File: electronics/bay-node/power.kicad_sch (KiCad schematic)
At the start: 23 parts, among them J1 24V IN, J2 24V OUT, Q1 SUD50P06-15, U1 LMR51635YDDCR, U2 AMS1117-3.3

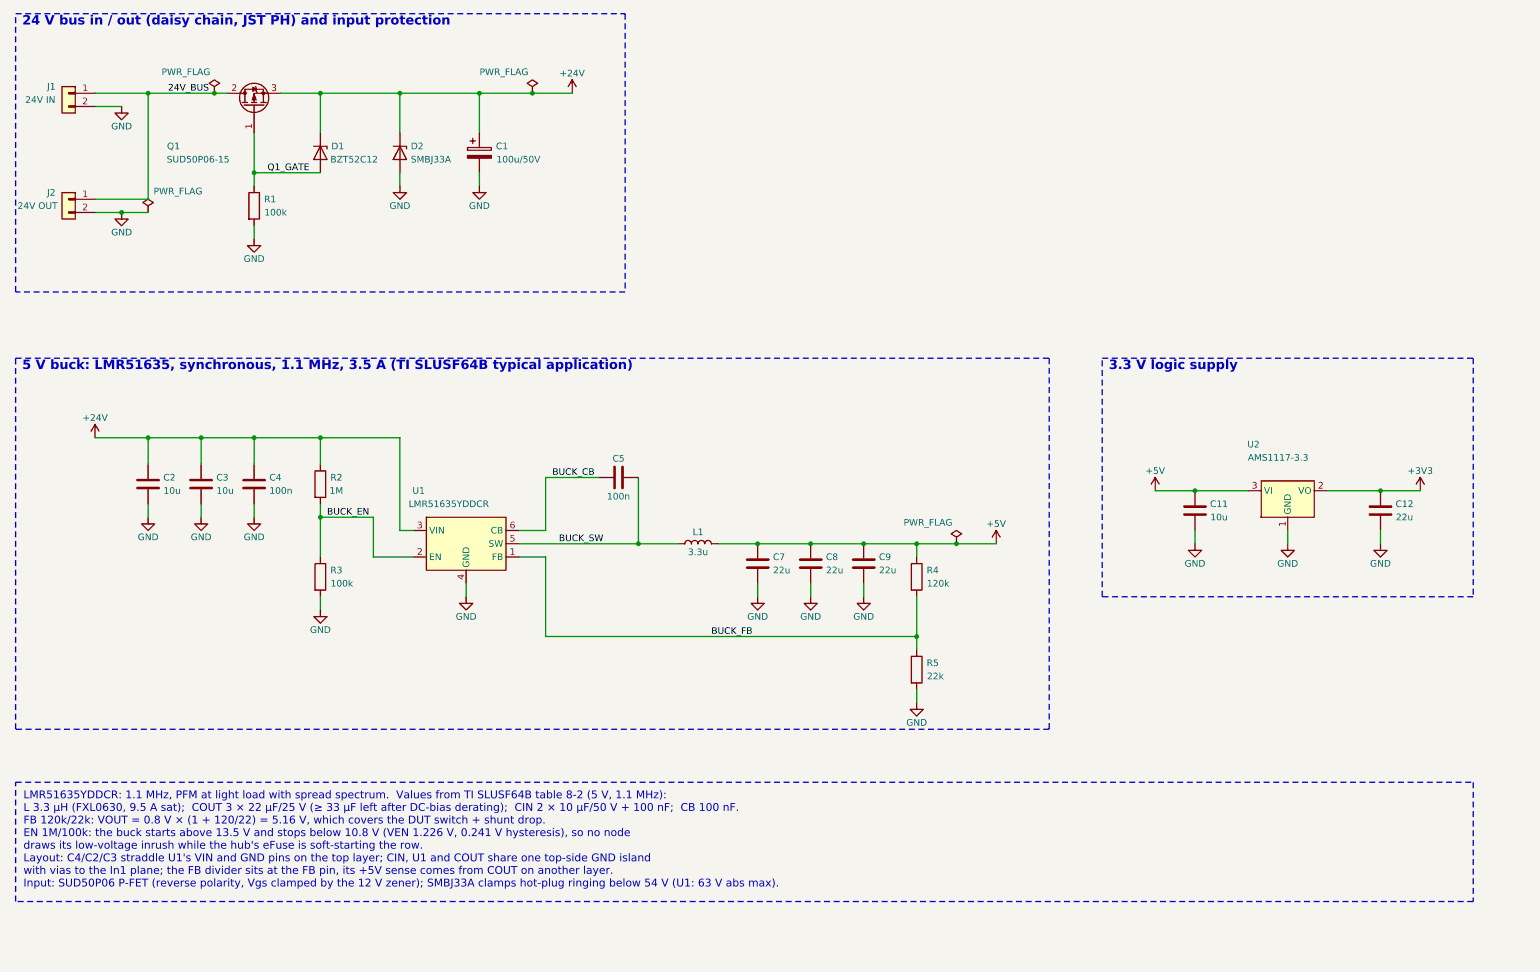
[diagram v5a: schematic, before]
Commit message: Bay node v0.5: 6-pin row cable with CAN and POS
The row cable becomes the docs/can.md contract: J1 (ROW IN, left) and J2 (ROW OUT,
right) are 6-pin JST PH S6B-PH-SM4-TB, +24 V, GND, CAN_H, CAN_L, GND, POS, with
pin 1 to the rear on the left edge and to the front on the right edge.

- Rack bus sheet: TCAN1044AV (VCC 5 V, VIO 3.3 V, STB low) right on the pair,
  which runs straight J1 -> J2 with no termination (stubs 1.8 / 2.3 mm),
  PESD2CAN on the tap; POS in through 10k + BAT54S + 100k pull-down, POS out
  through 10k + BAT54S.  TWAI on IO18/IO17, POS on IO16 (in) and IO35 (out).
- The input stage also takes a 20 / 28 V USB-C PD supply (notes on the Power
  sheet and in docs/electronics.md).
- Re-placed for In2 power only and autorouted: ERC 0, DRC 0, unconnected 0,
  parity 0 (kicad-cli and Konnect); no track on In1 or In2.
- JLC_CPL_FIX gains the rack bus parts, fitted on the EasyEDA footprints:
  S6B 180 deg, TCAN1044AV 270 deg, PESD2CAN and BAT54S 180 deg (they also apply
  to the power hub's row connectors, transceiver and clamps).
- Firmware: hwtr,rack-bus binding, TWAI pinctrl and node in the bay_node
  devicetree, check_pinmap and the README table; DevKitC moves POS_OUT to IO21,
  StampS3 disables the bus.  bay_node, DevKitC and StampS3 builds pass.
- Mechanics: the cable windows in the tray walls and the ladders widen to
  17 mm for the PHR-6 plug.  The viewer and the notice draw a 6-wire jumper.
- BOM: 6-pin jumpers; JLC_SINCE_QUOTE adds rev 0.5's parts and three extended
  part types to the node's quoted order (indicative, re-quote).

Regenerated: KiCad project, fab outputs, renders, schematic PDF, viewer GLB,
tray and ladder STLs, parts.glb, rack.json, bom/*.

Co-Authored-By: Claude Opus 5.5 <noreply@anthropic.com>
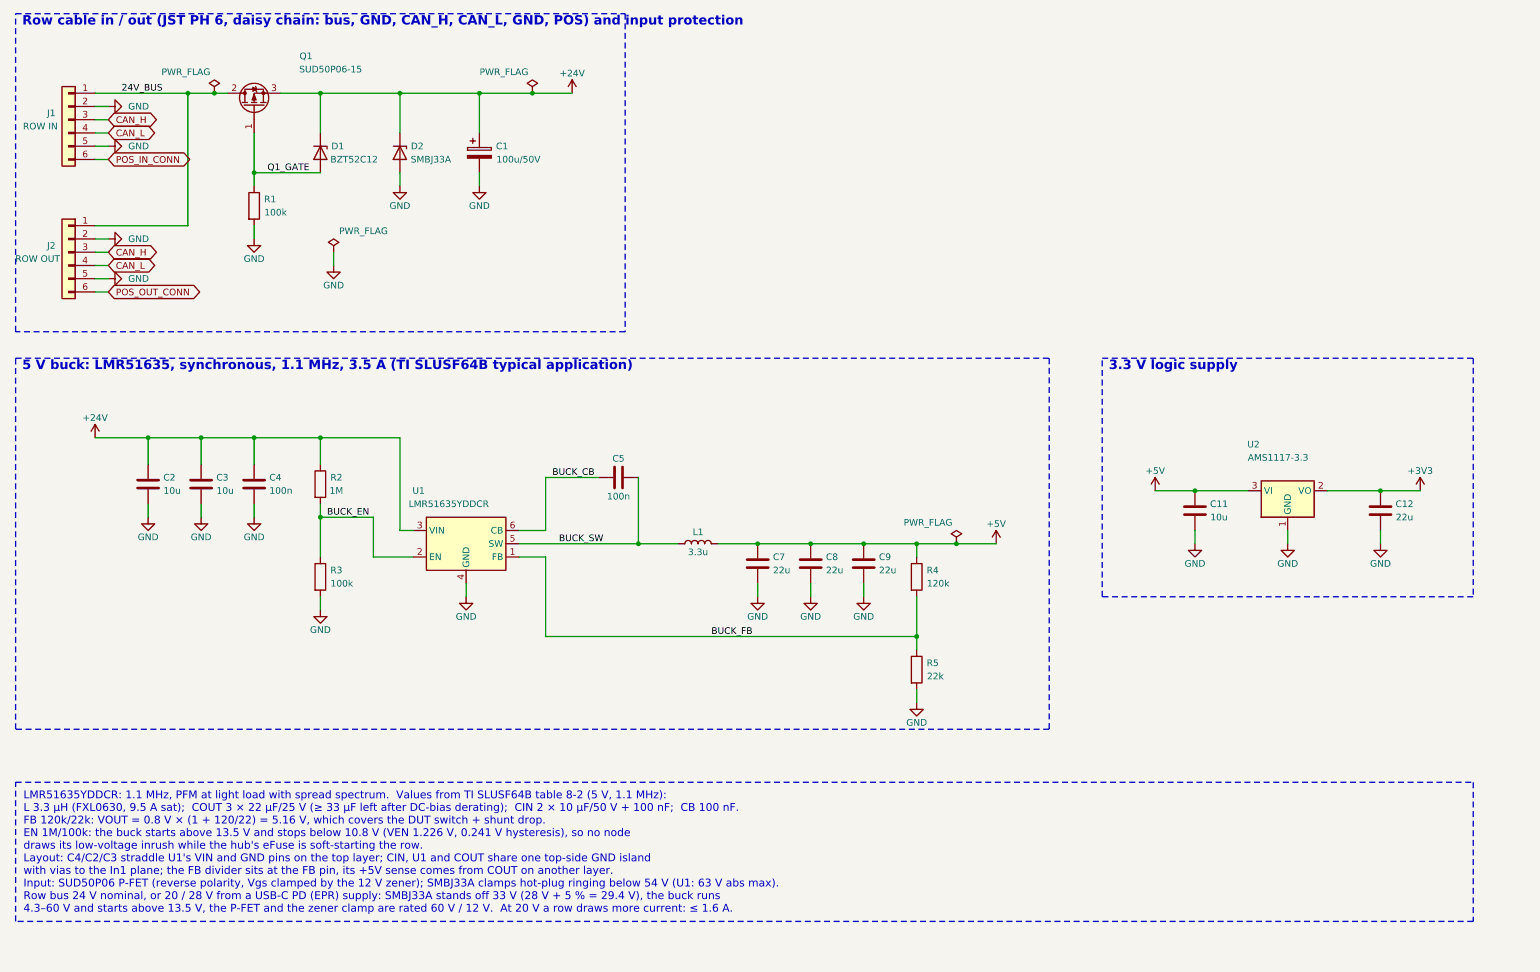
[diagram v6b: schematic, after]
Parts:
- J1: value 24V IN -> ROW IN; footprint Connector_JST:JST_PH_S2B-PH-SM4-TB_1x02-1MP_P2.00mm_Horizontal -> Connector_JST:JST_PH_S6B-PH-SM4-TB_1x06-1MP_P2.00mm_Horizontal; symbol Connector_Generic:Conn_01x02 -> Connector_Generic:Conn_01x06; LCSC C295747 -> C265405; MPN S2B-PH-SM4-TB(LF)(SN) -> S6B-PH-SM4-TB(LF)(SN)
- J2: value 24V OUT -> ROW OUT; footprint Connector_JST:JST_PH_S2B-PH-SM4-TB_1x02-1MP_P2.00mm_Horizontal -> Connector_JST:JST_PH_S6B-PH-SM4-TB_1x06-1MP_P2.00mm_Horizontal; symbol Connector_Generic:Conn_01x02 -> Connector_Generic:Conn_01x06; LCSC C295747 -> C265405; MPN S2B-PH-SM4-TB(LF)(SN) -> S6B-PH-SM4-TB(LF)(SN)
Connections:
- net GND: now also J1.5 (Pin_5), J2.5 (Pin_5)
- new net CAN_H: J1.3 (Pin_3), J2.3 (Pin_3)
- new net CAN_L: J1.4 (Pin_4), J2.4 (Pin_4)
- new net POS_IN_CONN: J1.6 (Pin_6)
- new net POS_OUT_CONN: J2.6 (Pin_6)
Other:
- note added: "Row cable in / out (JST PH 6, daisy chain: bus, GND, CAN_H, CAN_L, GND, POS) and input protection"
- note removed: "24 V bus in / out (daisy chain, JST PH) and input protection"

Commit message: Bay node v0.5: VRACK, GCT USB-C, VBUS caps on the ESD parts
Follows the power box's switch to USB-C PD (docs/can.md on the power-box branch):

- Pin 1 of the row cable is VRACK (20 V, or 28 V EPR): the net 24V_BUS becomes
  VRACK and +24V (after the P-FET) becomes VIN, in the schematic, the zones and
  the netclass patterns.  The input stage already takes 20-28 V.
- J3/J4 become the GCT USB4105-GF-A-120 (catalog usbc5a, LCSC C5184243), the
  part the user approved for the hub.  KiCad 10 ships its 3D model.  The pads
  sit 0.365 mm closer to the footprint origin than the HRO's, so the hand-drawn
  USB High-Speed tracks move with them (both lines of each pair alike, so the
  matching holds).  A board rule allows the footprint's own 0.19 mm between its
  GND pads and its pegs, the same rule the hub uses.
- Konnect's open point from v0.4: C25 and C26 (100 nF) on U4's and U8's VBUS.
- JLC_CPL_FIX: C5184243 at 0 deg, -1.30 mm y (EasyEDA fit, residual 0).
- JLC_SINCE_QUOTE: +$2.38 of parts per board ($38.10 for the 16 quoted).

ERC 0, DRC 0, unconnected 0, parity 0; Konnect's design review shows only the
known per-sheet false positives.  CAN stubs to U11: 2.2 / 7.9 mm.

Co-Authored-By: Claude Opus 5.5 <noreply@anthropic.com>
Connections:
- net +24V renamed VIN
- net 24V_BUS renamed VRACK
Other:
- title: Bay node — 24 V input, 5 V buck, 3.3 V LDO -> Bay node — VRACK input (20–28 V), 5 V buck, 3.3 V LDO
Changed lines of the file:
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@@
 	(paper "A3")
 	(title_block
-		(title "Bay node — 24 V input, 5 V buck, 3.3 V LDO")
+		(title "Bay node — VRACK input (20–28 V), 5 V buck, 3.3 V LDO")
 		(rev "0.5")
 		(company "hw-testing-rack")
@@
 		)
 	)
-	(symbol
-		(lib_id "power:+24V")
-		(at 121.92 30.48 0)
-		(unit 1)
-		(exclude_from_sim no)
-		(in_bom yes)
-		(on_board yes)
-		(dnp no)
+	(label "VIN"
+		(at 121.92 30.48 90)
 		(fields_autoplaced yes)
-		(property "Reference" "#PWR02021"
-			(at 121.92 30.48 0)
-			(effects
-				(font
-					(size 1.27 1.27)
-				)
-				(hide yes)
-			)
-		)
-		(property "Value" "+24V"
-			(at 121.92 26.67 0)
-			(effects
-				(font
-					(size 1.27 1.27)
-				)
-			)
-		)
-		(property "Footprint" ""
-			(at 121.92 30.48 0)
-			(effects
-				(font
-					(size 1.27 1.27)
-				)
-				(hide yes)
-			)
-		)
-		(property "Datasheet" ""
-			(at 121.92 30.48 0)
-			(effects
-				(font
-					(size 1.27 1.27)
-				)
-				(hide yes)
-			)
-		)
-		(property "Description" ""
-			(at 121.92 30.48 0)
-			(effects
-				(font
-					(size 1.27 1.27)
-				)
-				(hide yes)
-			)
-		)
-		(pin "1"
-		)
-		(instances
-			(project "bay-node"
-				(path "/76847c0c-2f76-566c-8109-428b2bf58b3f/6bdbf57d-f796-52cd-9884-75545352918b"
-					(reference "#PWR02021")
-					(unit 1)
-				)
+		(effects
+			(font
+				(size 1.27 1.27)
 			)
+			(justify left bottom)
 		)
 	)
-	(symbol
-		(lib_id "power:+24V")
-		(at 30.48 96.52 0)
-		(unit 1)
-		(exclude_from_sim no)
-		(in_bom yes)
-		(on_board yes)
-		(dnp no)
+	(label "VIN"
+		(at 30.48 96.52 90)
 		(fields_autoplaced yes)
-		(property "Reference" "#PWR02022"
-			(at 30.48 96.52 0)
-			(effects
-				(font
-					(size 1.27 1.27)
-				)
-				(hide yes)
-			)
-		)
-		(property "Value" "+24V"
-			(at 30.48 92.71 0)
-			(effects
-				(font
-					(size 1.27 1.27)
-				)
-			)
-		)
-		(property "Footprint" ""
-			(at 30.48 96.52 0)
-			(effects
-				(font
-					(size 1.27 1.27)
-				)
-				(hide yes)
-			)
-		)
-		(property "Datasheet" ""
-			(at 30.48 96.52 0)
-			(effects
-				(font
-					(size 1.27 1.27)
-				)
-				(hide yes)
-			)
-		)
-		(property "Description" ""
-			(at 30.48 96.52 0)
-			(effects
-				(font
-					(size 1.27 1.27)
-				)
-				(hide yes)
-			)
-		)
-		(pin "1"
-		)
-		(instances
-			(project "bay-node"
-				(path "/76847c0c-2f76-566c-8109-428b2bf58b3f/6bdbf57d-f796-52cd-9884-75545352918b"
-					(reference "#PWR02022")
-					(unit 1)
-				)
+		(effects
+			(font
+				(size 1.27 1.27)
 			)
+			(justify left bottom)
 		)
 	)
@@
 		(dnp no)
 		(fields_autoplaced yes)
-		(property "Reference" "#PWR02023"
+		(property "Reference" "#PWR02021"
 			(at 203.2 116.84 0)
 			(effects
@@
 			(project "bay-node"
 				(path "/76847c0c-2f76-566c-8109-428b2bf58b3f/6bdbf57d-f796-52cd-9884-75545352918b"
-					(reference "#PWR02023")
+					(reference "#PWR02021")
 					(unit 1)
 				)
@@
 		(dnp no)
 		(fields_autoplaced yes)
-		(property "Reference" "#PWR02024"
+		(property "Reference" "#PWR02022"
 			(at 233.68 106.68 0)
 			(effects
@@
 			(project "bay-node"
 				(path "/76847c0c-2f76-566c-8109-428b2bf58b3f/6bdbf57d-f796-52cd-9884-75545352918b"
-					(reference "#PWR02024")
+					(reference "#PWR02022")
 					(unit 1)
 				)
@@
 		(dnp no)
 		(fields_autoplaced yes)
-		(property "Reference" "#PWR02025"
+		(property "Reference" "#PWR02023"
 			(at 284.48 106.68 0)
 			(effects
@@
 			(project "bay-node"
 				(path "/76847c0c-2f76-566c-8109-428b2bf58b3f/6bdbf57d-f796-52cd-9884-75545352918b"
-					(reference "#PWR02025")
+					(reference "#PWR02023")
 					(unit 1)
 				)
@@
 		)
 	)
-	(label "24V_BUS"
-		(at 35.56 30.48 0)
+	(label "VRACK"
+		(at 36.83 30.48 0)
 		(fields_autoplaced yes)
 		(effects
@@
 		)
 	)
-	(text_box "LMR51635YDDCR: 1.1 MHz, PFM at light load with spread spectrum.  Values from TI SLUSF64B table 8-2 (5 V, 1.1 MHz):\n  L 3.3 µH (FXL0630, 9.5 A sat);  COUT 3 × 22 µF/25 V (≥ 33 µF left after DC-bias derating);  CIN 2 × 10 µF/50 V + 100 nF;  CB 100 nF.\nFB 120k/22k: VOUT = 0.8 V × (1 + 120/22) = 5.16 V, which covers the DUT switch + shunt drop.\nEN 1M/100k: the buck starts above 13.5 V and stops below 10.8 V (VEN 1.226 V, 0.241 V hysteresis), so no node\n  draws its low-voltage inrush while the hub's eFuse is soft-starting the row.\nLayout: C4/C2/C3 straddle U1's VIN and GND pins on the top layer; CIN, U1 and COUT share one top-side GND island\n  with vias to the In1 plane; the FB divider sits at the FB pin, its +5V sense comes from COUT on another layer.\nInput: SUD50P06 P-FET (reverse polarity, Vgs clamped by the 12 V zener); SMBJ33A clamps hot-plug ringing below 54 V (U1: 63 V abs max).\nRow bus 24 V nominal, or 20 / 28 V from a USB-C PD (EPR) supply: SMBJ33A stands off 33 V (28 V + 5 % = 29.4 V), the buck runs\n  4.3–60 V and starts above 13.5 V, the P-FET and the zener clamp are rated 60 V / 12 V.  At 20 V a row draws more current: ≤ 1.6 A."
+	(text_box "LMR51635YDDCR: 1.1 MHz, PFM at light load with spread spectrum.  Values from TI SLUSF64B table 8-2 (5 V, 1.1 MHz):\n  L 3.3 µH (FXL0630, 9.5 A sat);  COUT 3 × 22 µF/25 V (≥ 33 µF left after DC-bias derating);  CIN 2 × 10 µF/50 V + 100 nF;  CB 100 nF.\nFB 120k/22k: VOUT = 0.8 V × (1 + 120/22) = 5.16 V, which covers the DUT switch + shunt drop.\nEN 1M/100k: the buck starts above 13.5 V and stops below 10.8 V (VEN 1.226 V, 0.241 V hysteresis), so no node\n  draws its low-voltage inrush while the hub's eFuse is soft-starting the row.\nLayout: C4/C2/C3 straddle U1's VIN and GND pins on the top layer; CIN, U1 and COUT share one top-side GND island\n  with vias to the In1 plane; the FB divider sits at the FB pin, its +5V sense comes from COUT on another layer.\nInput: SUD50P06 P-FET (reverse polarity, Vgs clamped by the 12 V zener); SMBJ33A clamps hot-plug ringing below 54 V (U1: 63 V abs max).\nVRACK is 20 V, or 28 V (EPR), from the hub's USB-C PD supply: SMBJ33A stands off 33 V (28 V + 5 % = 29.4 V), the buck runs\n  4.3–60 V and starts above 13.5 V, the P-FET and the zener clamp are rated 60 V / 12 V.  At 20 V a row draws more current: ≤ 1.6 A."
 		(exclude_from_sim no)
 		(at 15.24 162.56 0)

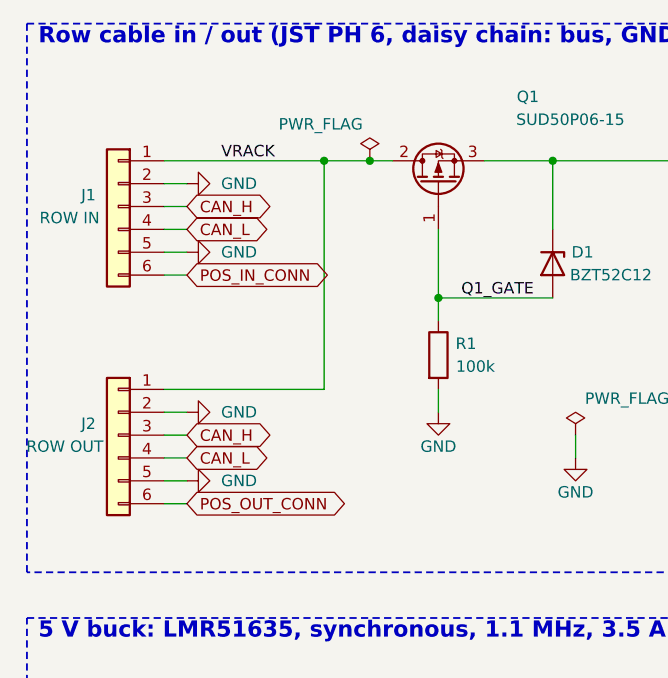
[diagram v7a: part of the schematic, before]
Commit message: Row cable without a twist: J2 mirrored on the bay node
J1 and J2 are the same side-entry footprint turned 180°, so with one pinout
on both, the 1:1 jumper between two nodes had to make a half twist.  J2 now
carries J1's pinout mirrored (J2.n = J1.(7-n): 1 POS out, 2 GND, 3 CAN_L,
4 CAN_H, 5 GND, 6 VRACK):

* the jumper lies flat: pin n to pin 7-n, both plugs the same face up;
* every net crosses the node straight: the In2 VRACK strip runs from J1.1
  to J2.6 at the same height, and R30 sits by J2.1;
* the hub keeps J1's pinout and the feeds stay 1:1: out of the box's left
  wall and back into J1 from the left, they fold over once;
* a wrong cable burns nothing: VRACK lands on a POS pin (10k + BAT54S),
  CAN swaps, and the next node stays off.

The node is re-routed: ERC 0, DRC 0, unconnected 0, parity 0; CAN stubs
≤ 8.2 mm; 85 3D models, 0 stand-ins.  docs/can.md (the contract),
cabling.md, electronics.md, the Konnect review, the BOM cable lines and the
viewer's jumper (flat again) follow.

Co-Authored-By: Claude Opus 5.5 <noreply@anthropic.com>
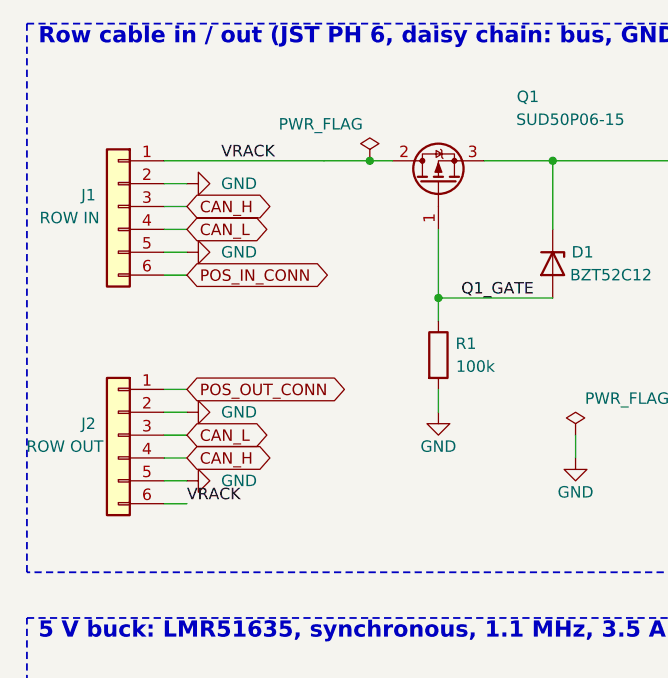
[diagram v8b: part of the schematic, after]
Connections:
- net CAN_H: now also J2.4 (Pin_4); no longer J2.3 (Pin_3)
- net CAN_L: now also J2.3 (Pin_3); no longer J2.4 (Pin_4)
- net POS_OUT_CONN: now also J2.1 (Pin_1); no longer J2.6 (Pin_6)
- net VRACK: now also J2.6 (Pin_6); no longer J2.1 (Pin_1)
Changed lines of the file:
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@@
+	(wire
+		(pts
+			(xy 30.48 55.88)
+			(xy 33.02 55.88)
+		)
+		(stroke
+			(width 0)
+			(type default)
+		)
+	)
 	(wire
 		(pts
@@
 	(wire
 		(pts
-			(xy 30.48 55.88)
-			(xy 48.26 55.88)
-		)
-		(stroke
-			(width 0)
-			(type default)
-		)
-	)
-	(wire
-		(pts
-			(xy 48.26 55.88)
-			(xy 48.26 30.48)
-		)
-		(stroke
-			(width 0)
-			(type default)
-		)
-	)
-	(wire
-		(pts
 			(xy 76.2 60.96)
 			(xy 76.2 63.5)
@@
 	(junction
 		(at 40.64 96.52)
-		(diameter 0)
-		(color 0 0 0 0)
-	)
-	(junction
-		(at 48.26 30.48)
 		(diameter 0)
 		(color 0 0 0 0)
@@
 		)
 	)
-	(global_label "CAN_H"
+	(global_label "CAN_L"
 		(shape bidirectional)
 		(at 33.02 60.96 0)
@@
 		)
 	)
-	(global_label "CAN_L"
+	(global_label "CAN_H"
 		(shape bidirectional)
 		(at 33.02 63.5 0)
@@
 		)
 	)
-	(global_label "POS_OUT_CONN"
-		(shape bidirectional)
+	(label "VRACK"
 		(at 33.02 68.58 0)
 		(fields_autoplaced yes)
@@
 				(size 1.27 1.27)
 			)
+			(justify left bottom)
+		)
+	)
+	(global_label "POS_OUT_CONN"
+		(shape bidirectional)
+		(at 33.02 55.88 0)
+		(fields_autoplaced yes)
+		(effects
+			(font
+				(size 1.27 1.27)
+			)
 			(justify left)
 		)
 		(property "Intersheetrefs" "${INTERSHEET_REFS}"
-			(at 33.02 68.58 0)
-			(effects
-				(font
+			(at 33.02 55.88 0)
+			(effects
+				(font
